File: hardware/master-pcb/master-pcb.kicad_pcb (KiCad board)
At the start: 4 copper layers, 84 x 69 mm, 37 parts, among them J1 RS-485 OUT, J2 INT IN 0-8, J4 UNDERGLOW OUT, SW1 PLAYER_ID, U1 Teensy 4.0, U2 THVD1429, U3 SN74AHCT125

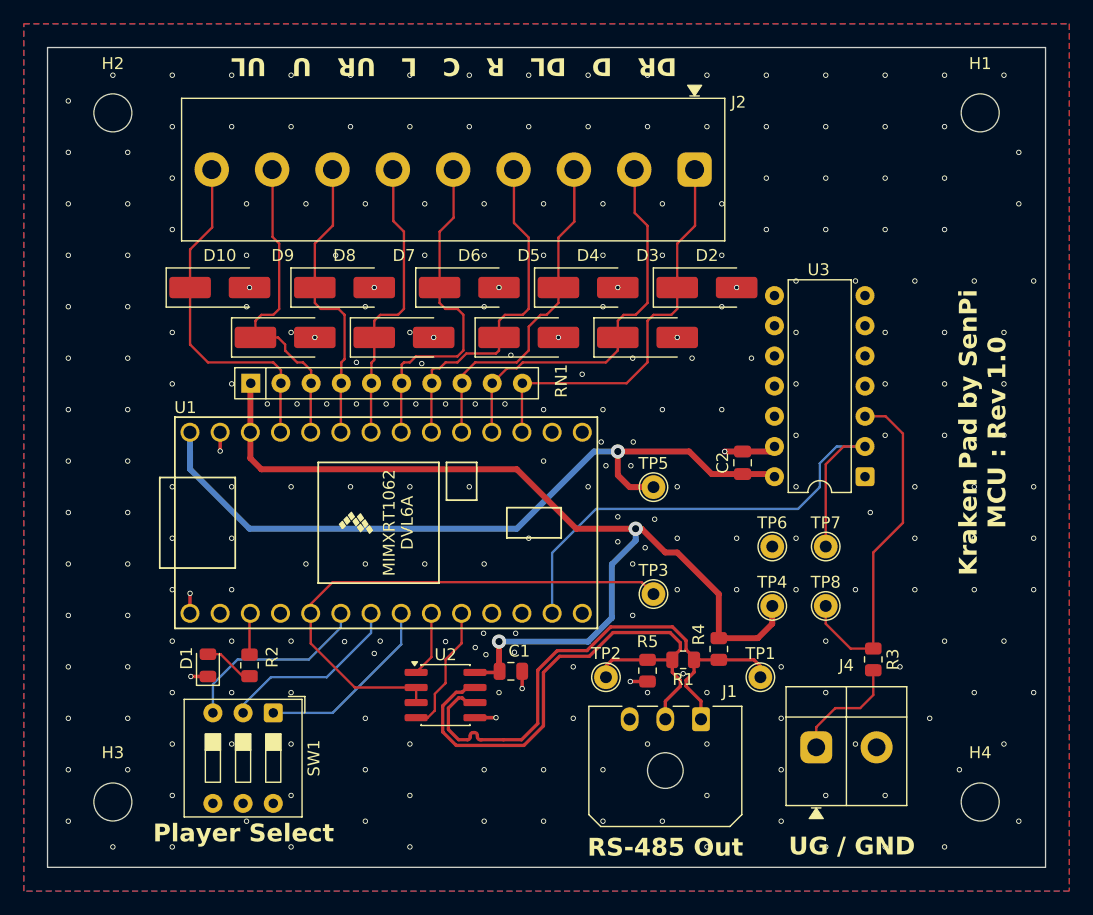
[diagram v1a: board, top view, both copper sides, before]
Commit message: Master: post-review rework — remove status LED, INT RC/TVS filter, pin reassign
- Remove status LED (D1, R2); Teensy onboard LED (pin 13) serves as status
- INT lines get two-stage protection: SMAJ5.0A TVS at the J2 entry + 330R
  series (R6-R14) + 1nF C0G RC (C3-C11) to GND on the Teensy-side node.
  Resolves review F3/F4 (series R makes the 5V-standoff TVS safe on the
  non-5V-tolerant Teensy pin; RC filters ESD/EMI). Pull-up stays Teensy-side.
- R15 10k pull-down on UNDERGLOW_DATA — defines U3 gate-A input LOW at boot
  (review F5)
- DIP -> GPIO 3/4/5, RS485_DE -> GPIO6; frees GPIO 0/1/2 and keeps Serial1
  (0/1) as the last spare hardware UART. RS-485 stays on Serial2 (7/8).
- ERC/DRC clean. docs/MASTER_PCB.md + BOM.md updated to match.
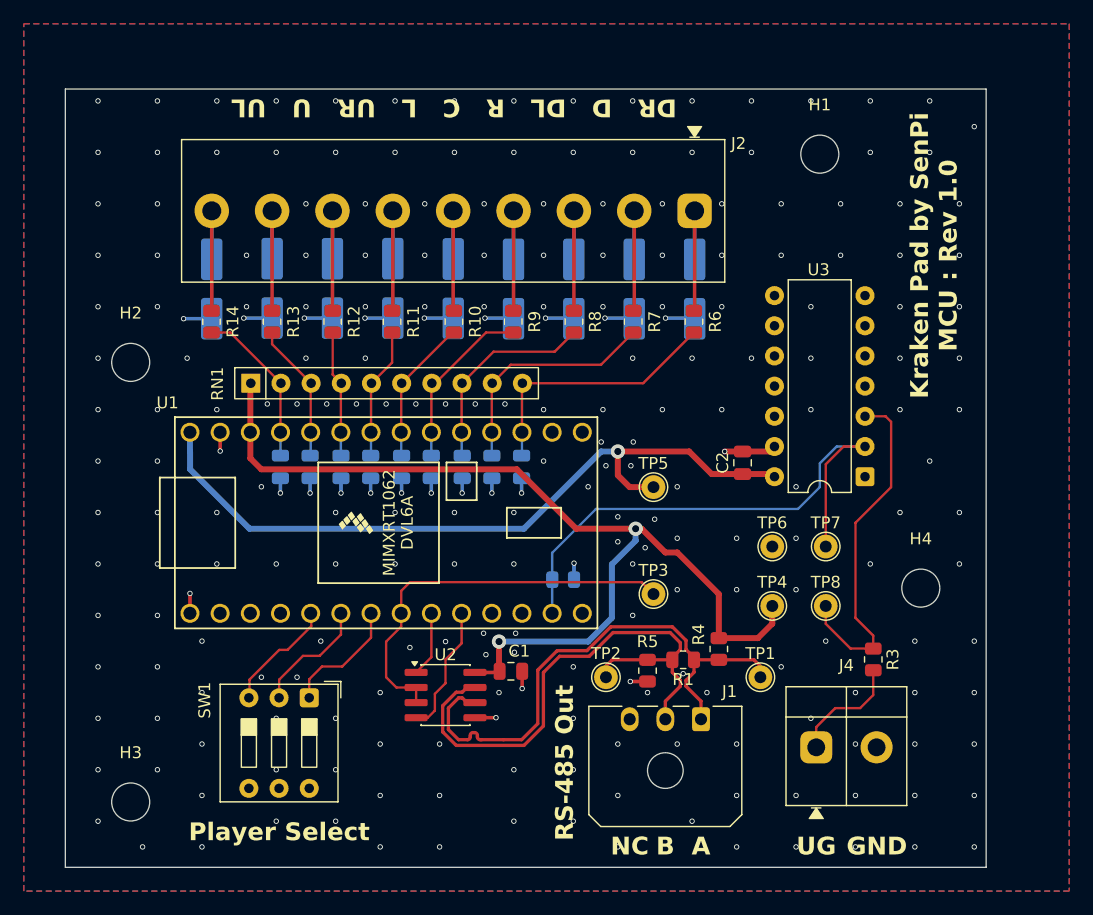
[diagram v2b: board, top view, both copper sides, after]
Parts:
- removed D1: STATUS, LED_SMD:LED_0805_2012Metric
- removed R2: 1k, Resistor_SMD:R_0805_2012Metric
- added C10: 1nF C0G, Capacitor_SMD:C_0805_2012Metric, B.Cu at (111.6, 109.3)
- added C11: 1nF C0G, Capacitor_SMD:C_0805_2012Metric, B.Cu at (109.1, 109.3)
- added C3: 1nF C0G, Capacitor_SMD:C_0805_2012Metric, B.Cu at (129.4, 109.3)
- added C4: 1nF C0G, Capacitor_SMD:C_0805_2012Metric, B.Cu at (126.9, 109.3)
- added C5: 1nF C0G, Capacitor_SMD:C_0805_2012Metric, B.Cu at (124.4, 109.3)
- added C6: 1nF C0G, Capacitor_SMD:C_0805_2012Metric, B.Cu at (121.8, 109.3)
- added C7: 1nF C0G, Capacitor_SMD:C_0805_2012Metric, B.Cu at (119.3, 109.3)
- added C8: 1nF C0G, Capacitor_SMD:C_0805_2012Metric, B.Cu at (116.7, 109.3)
- added C9: 1nF C0G, Capacitor_SMD:C_0805_2012Metric, B.Cu at (114.2, 109.3)
- added R10: 330R, Resistor_SMD:R_0805_2012Metric, F.Cu at (123.7, 97.1)
- added R11: 330R, Resistor_SMD:R_0805_2012Metric, F.Cu at (118.5, 97.1)
- added R12: 330R, Resistor_SMD:R_0805_2012Metric, F.Cu at (113.5, 97.1)
- added R13: 330R, Resistor_SMD:R_0805_2012Metric, F.Cu at (108.4, 97.1)
- added R14: 330R, Resistor_SMD:R_0805_2012Metric, F.Cu at (103.3, 97.1)
- added R15: 10k, Resistor_SMD:R_0805_2012Metric, B.Cu at (132.9, 118.8)
- added R6: 330R, Resistor_SMD:R_0805_2012Metric, F.Cu at (143.9, 97.1)
- added R7: 330R, Resistor_SMD:R_0805_2012Metric, F.Cu at (138.8, 97.1)
- added R8: 330R, Resistor_SMD:R_0805_2012Metric, F.Cu at (133.8, 97.1)
- added R9: 330R, Resistor_SMD:R_0805_2012Metric, F.Cu at (128.7, 97.1)
- D10, D2, D3, D4, D5, D6, D7, D8, D9: moved to B.Cu
- moved H2 21.1 mm to (96.5, 100.5)
- moved H4 18.7 mm to (163.0, 119.5)
- moved H1 13.9 mm to (154.5, 83.0)
- moved D9 4.27 mm to (108.4, 94.3), turned to -90 degrees
- moved D5 4.27 mm to (128.7, 94.3), turned to -90 degrees
- moved D7 4.23 mm to (118.6, 94.3), turned to -90 degrees
- moved D3 4.22 mm to (138.9, 94.3), turned to -90 degrees
- moved J2 3.47 mm to (144.0, 87.7)
- moved SW1 3.28 mm to (111.5, 128.7)
- moved H3 1.50 mm to (96.5, 137.5)
- moved D6 1.36 mm to (123.6, 94.3), turned to -90 degrees
- moved D4 1.20 mm to (133.8, 94.3), turned to -90 degrees
- moved D2 1.04 mm to (144.0, 94.3), turned to -90 degrees
- moved D8 1.02 mm to (113.5, 94.3), turned to -90 degrees
- moved D10 0.69 mm to (103.3, 94.3), turned to -90 degrees
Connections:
- D10 pad 1: INT_UL -> Net-(D10-K)
- D2 pad 1: INT_DR -> Net-(D2-K)
- D3 pad 1: INT_D -> Net-(D3-K)
- D4 pad 1: INT_DL -> Net-(D4-K)
- D5 pad 1: INT_R -> Net-(D5-K)
- D6 pad 1: INT_C -> Net-(D6-K)
- D7 pad 1: INT_L -> Net-(D7-K)
- D8 pad 1: INT_UR -> Net-(D8-K)
- D9 pad 1: INT_U -> Net-(D9-K)
- J2 pad 1: INT_DR -> Net-(D2-K)
- J2 pad 2: INT_D -> Net-(D3-K)
- J2 pad 3: INT_DL -> Net-(D4-K)
- J2 pad 4: INT_R -> Net-(D5-K)
- J2 pad 5: INT_C -> Net-(D6-K)
- J2 pad 6: INT_L -> Net-(D7-K)
- J2 pad 7: INT_UR -> Net-(D8-K)
- J2 pad 8: INT_U -> Net-(D9-K)
- J2 pad 9: INT_UL -> Net-(D10-K)
- U1 pad 3: /STATUS_LED -> unconnected-(U1-GPIO_1-Pad3)
- U1 pad 5: RS485_DE -> /DIP_ID2
- U1 pad 6: /DIP_ID2 -> /DIP_ID1
- U1 pad 7: /DIP_ID1 -> /DIP_ID0
- U1 pad 8: /DIP_ID0 -> RS485_DE
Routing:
- net GND: track 13.7 -> 46.3 mm, vias 264 -> 244
- net INT_C: track 28.5 -> 12.3 mm
- net INT_UL: track 29.3 -> 13.7 mm
- net INT_U: track 27.1 -> 11.8 mm
- net INT_R: track 29.2 -> 14.7 mm
- net INT_UR: track 24.8 -> 10.7 mm
- net INT_L: track 24.5 -> 11.1 mm
- net INT_D: track 33.1 -> 19.7 mm
- net Net-(D3-K): track 0.00 -> 12.5 mm
- net Net-(D2-K): track 0.00 -> 12.5 mm
- net Net-(D5-K): track 0.00 -> 12.5 mm
- net Net-(D10-K): track 0.00 -> 12.5 mm
- net Net-(D4-K): track 0.00 -> 12.5 mm
- net Net-(D6-K): track 0.00 -> 12.5 mm
- net Net-(D7-K): track 0.00 -> 12.5 mm
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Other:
- board size 84 x 69 mm -> 77.5 x 65.5 mm
- board text added: "A"
- board text added: "B"
- board text added: "GND"
- board text added: "NC"
- board text added: "UG"
- board text removed: "UG / GND"

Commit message: Master: RS-485 pair length-matched, RX/TX test points added
Same stackup as the panel (JLC04161H-7628), so the same 120-ohm target
geometry applies. The pair was already at W=0.15/S=0.2 -- it landed on the
right answer via the 0.15mm data-trace convention rather than by calculation
-- so only the skew needed work.

- /RS485+ and /RS485- now 45.39mm each: 0.000mm skew (was 0.60mm). F.Cu only,
  zero vias, ~119 ohm. Netclass diff-pair width corrected 0.2787 -> 0.15 and
  the stale USB pair class dropped (the Teensy handles USB internally; nothing
  USB is routed on this board).
- TP9 (RS485_RX) and TP10 (RS485_TX) added, giving probe access to the full
  transceiver interface alongside TP1/TP2/TP3 (A/B/DE).
- ~69% of the run is coupled at 0.2mm; the rest fans out to reach pads that
  are farther apart than the pair pitch (U2 pins 6/7, J1 Micro-Fit, R1,
  TP1/TP2). That is unavoidable and inconsequential at 1 Mbps -- documented as
  do-not-fix so it is not "corrected" later.

Also recorded: both inner layers are GND (GND_1/GND_2), unlike the panel's
GND/power split, so there is no reference-plane-type change anywhere on this
board.

Verified with all three ignored severities lifted, --severity-all
--schematic-parity --refill-zones: 0 violations, 0 unconnected, ERC 0. Only 3
cosmetic footprint_filters_mismatch notes (Euroblock, MRR52, DIP-3).
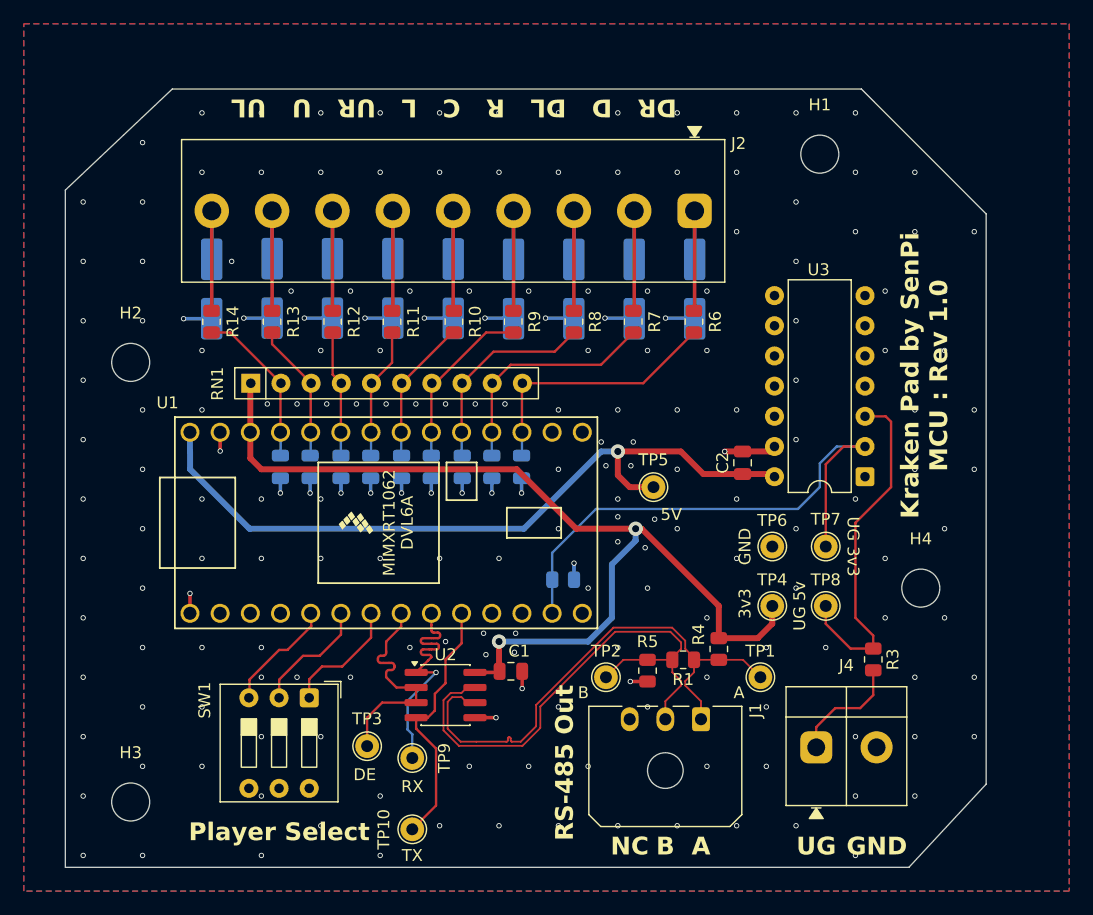
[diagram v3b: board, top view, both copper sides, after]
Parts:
- added TP10: RS-485 TX, TestPoint:TestPoint_THTPad_D2.0mm_Drill1.0mm, F.Cu at (120.2, 139.8)
- added TP9: RS-485 RX, TestPoint:TestPoint_THTPad_D2.0mm_Drill1.0mm, F.Cu at (120.2, 133.8)
- moved TP3 27.3 mm to (116.4, 132.8)
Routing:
- net RS485_RX: track 5.51 -> 20.9 mm, vias 0 -> 1
- net RS485_DE: track 33.9 -> 19.2 mm
- net RS485_TX: track 10.9 -> 21.9 mm
- net /RS485-: track 47.2 -> 45.4 mm
- net /RS485+: track 47.2 -> 45.4 mm
- net +3.3VDC: track 84.0 -> 83.3 mm
- net GND: vias 244 -> 201
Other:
- outline, holes or cut-outs redrawn
- board text added: "3v3"
- board text added: "5V"
- board text added: "DE"
- board text added: "RX"
- board text added: "TX"
- board text added: "UG 3v3"
- board text added: "UG 5v"

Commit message: Both boards: J9/J4 to the vendor WJ500V land pattern; WS2815 cap question closed
Terminal blocks now use the footprint published by the manufacturer of the part
we actually buy (KANGNEX WJ500V-5.08-2P, LCSC C8465), pulled via easyeda2kicad,
replacing the hand-built Adam Tech MRR52 pattern:
- new panel-pcb/master-pcb:TerminalBlock_WJ500V-5.08-2P (hole 1.30mm per the
  vendor recommendation vs our 1.50mm, pad 2.00mm, origin centred between pins)
  plus the vendor 3D model, which supersedes the Phoenix MKDS stand-in
- panel J9 and master J4 reassigned, re-placed and re-routed
- part metadata follows: MPN WJ500V-5.08-2P, LCSC C8465, datasheet to the LCSC
  page, stale DigiKey fields dropped

Pitch (5.08mm) and body envelope (10.16 x 10.16mm) came out of the vendor data
matching our drawing-derived numbers, so that part of the physical-verification
item is closed without parts in hand; pin-1 orientation still wants an eyeball
on arrival.

Checklist: WS2815 5V bench test waived (not worth buying parts; the substantive
check was the datasheet-variant confirm, and VIH 2.7V min is a spec guarantee).
Per-LED pin-1 caps C22-C49 CLOSED as correct — the original 2018 WS2815 doc and
WS2815B-V3 both give pin 1 as "IC POWER SUPPLY, Suspended or connected with a
filter capacitor to GROUND"; our V1 doc is the outlier calling it NC. Paper does
not prove V1 silicon brings that rail out, but a 100nF is no DC load, so the cap
is inert at worst. No per-LED VDD decoupling is wanted: the channels are
constant-current, and the vendor states no extra components are needed.

DRC 0 / schematic-parity 0 / ERC 0 on both boards, zero exclusions.
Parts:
- J4: footprint master-pcb:TerminalBlock_MRR52-5.08-2P -> master-pcb:TerminalBlock_WJ500V-5.08-2P
- moved J4 2.53 mm to (156.7, 132.9), turned to 180 degrees
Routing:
- net Net-(J4-Pin_1): track 9.71 -> 6.60 mm
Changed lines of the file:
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@@
 		)
 	)
-	(footprint "master-pcb:TerminalBlock_MRR52-5.08-2P"
+	(footprint "master-pcb:TerminalBlock_WJ500V-5.08-2P"
 		(layer "F.Cu")
-		(at 154.2 132.9)
-		(descr "Adam Tech MRR52-5.08-V, 2-position Eurostyle PCB screw terminal block, 5.08mm pitch. Dims from datasheet 375571 (2020/01): body 10.16 x 10.00mm, pin row 5.10mm from wire-entry face, PCB hole Rec. dia 1.50mm.")
-		(tags "terminal block MRR52 euroblock 5.08mm screw")
+		(at 156.7275 132.9 180)
+		(descr "KANGNEX WJ500V-5.08-2P, 2-position Eurostyle PCB screw terminal block, 5.08mm pitch (LCSC C8465). Land pattern and 3D model are the VENDOR's own, pulled via easyeda2kicad 2026-07-26 -- this replaces the hand-built TerminalBlock_MRR52-5.08-2P (Adam Tech drawing, 1.5mm holes) now that the part is sourced from LCSC. Recommended hole 1.30mm, pad 2.00mm (annular ring 0.35mm, vs the 0.15mm .dru minimum). Body 10.16 x 10.16mm; the pin row is NOT centred -- 5.64mm to the wire-entry face (-Y, marked by the silk arrows) and 4.52mm to the back. Origin is centred between the two pins.")
+		(tags "terminal block WJ500V euroblock 5.08mm screw KANGNEX")
 		(property "Reference" "J4"
-			(at 2.54 -6.9 0)
+			(at 6.2275 -4.9 90)
 			(layer "F.SilkS")
 			(effects
@@
 		)
 		(property "Value" "UNDERGLOW OUT"
-			(at 2.54 6.4 0)
+			(at 0 5.9 0)
 			(layer "F.Fab")
 			(effects
@@
 			)
 		)
-		(property "Datasheet" "https://dcomponents.com/uploads/375571_MRR52-5.08-V.pdf"
+		(property "Datasheet" "https://www.lcsc.com/product-detail/C8465.html"
 			(at 0 0 0)
 			(layer "F.Fab")
@@
 			)
 		)
-		(property "Description" "Adam Tech MRR522-5.08-V, 2P 5.08mm top-entry screw terminal: GND + LED-DATA-OUT (5V logic). UI-gated; no sense pin"
+		(property "Description" "KANGNEX WJ500V-5.08-2P (LCSC C8465), 2P 5.08mm top-entry screw terminal: GND + LED-DATA-OUT (5V logic). UI-gated; no sense pin"
 			(at 0 0 0)
 			(layer "F.Fab")
@@
 			)
 		)
-		(property "LCSC" ""
+		(property "LCSC" "C8465"
 			(at 0 0 0)
-			(unlocked yes)
 			(layer "F.Fab")
 			(hide yes)
 			(effects
 				(font
-					(size 1 1)
-					(thickness 0.15)
-				)
-			)
-		)
-		(property "MPN" "MRR522-5.08-V"
-			(at 0 0 0)
-			(unlocked yes)
-			(layer "F.Fab")
-			(hide yes)
-			(effects
-				(font
-					(size 1 1)
+					(size 1.27 1.27)
 					(thickness 0.15)
 				)
 			)
 		)
-		(property "DigiKey" "5245-MRR522-5.08-V-ND"
-			(at 0 0 0)
+		(property "MPN" "WJ500V-5.08-2P"
+			(at 0 0 180)
 			(unlocked yes)
 			(layer "F.Fab")
@@
 		(duplicate_pad_numbers_are_jumpers no)
 		(fp_line
-			(start -2.54 -5.1)
-			(end 7.62 -5.1)
-			(stroke
-				(width 0.12)
-				(type solid)
-			)
-			(layer "F.SilkS")
-		)
-		(fp_line
-			(start -2.54 -2.55)
-			(end 7.62 -2.55)
+			(start 5.08 4.52)
+			(end -5.08 4.52)
 			(stroke
 				(width 0.12)
@@
 		)
 		(fp_line
-			(start -2.54 4.9)
-			(end -2.54 -5.1)
+			(start 5.08 -5.64)
+			(end 5.08 4.52)
 			(stroke
 				(width 0.12)
@@
 		)
 		(fp_line
-			(start 0.4 5.1)
-			(end -0.4 5.1)
+			(start 0 -5.64)
+			(end 0 4.52)
 			(stroke
 				(width 0.12)
@@
 		)
 		(fp_line
-			(start 2.54 -5.1)
-			(end 2.54 4.9)
+			(start -5.08 4.52)
+			(end -5.08 -5.64)
 			(stroke
 				(width 0.12)
@@
 		)
 		(fp_line
-			(start 7.62 -5.1)
-			(end 7.62 4.9)
+			(start -5.08 -2.55)
+			(end 5.08 -2.55)
 			(stroke
 				(width 0.12)
@@
 		)
 		(fp_line
-			(start 7.62 4.9)
-			(end -2.54 4.9)
+			(start -5.08 -5.64)
+			(end 5.08 -5.64)
 			(stroke
 				(width 0.12)
@@
 			(layer "F.SilkS")
 		)
-		(fp_poly
-			(pts
-				(xy -0.6 6) (xy 0 5.1) (xy 0.6 6)
-			)
+		(fp_circle
+			(center -6.1 4.52)
+			(end -5.85 4.52)
 			(stroke
-				(width 0.1)
+				(width 0.3)
 				(type solid)
 			)
@@
 		)
 		(fp_line
-			(start -2.79 -5.35)
-			(end 7.87 -5.35)
+			(start 5.33 4.77)
+			(end -5.33 4.77)
 			(stroke
 				(width 0.05)
@@
 		)
 		(fp_line
-			(start -2.79 5.15)
-			(end -2.79 -5.35)
+			(start 5.33 -5.89)
+			(end 5.33 4.77)
 			(stroke
 				(width 0.05)
@@
 		)
 		(fp_line
-			(start 7.87 -5.35)
-			(end 7.87 5.15)
+			(start -5.33 4.77)
+			(end -5.33 -5.89)
 			(stroke
 				(width 0.05)
@@
 		)
 		(fp_line
-			(start 7.87 5.15)
-			(end -2.79 5.15)
+			(start -5.33 -5.89)
+			(end 5.33 -5.89)
 			(stroke
 				(width 0.05)
@@
 		)
 		(fp_line
-			(start -2.54 -5.1)
-			(end 7.62 -5.1)
+			(start 5.08 4.52)
+			(end -5.08 4.52)
 			(stroke
 				(width 0.1)
@@
 		)
 		(fp_line
-			(start -2.54 4.9)
-			(end -2.54 -5.1)
+			(start 5.08 -5.64)
+			(end 5.08 4.52)
 			(stroke
 				(width 0.1)
@@
 		)
 		(fp_line
-			(start 7.62 -5.1)
-			(end 7.62 4.9)
+			(start -5.08 4.52)
+			(end -5.08 -5.64)
 			(stroke
 				(width 0.1)
@@
 		)
 		(fp_line
-			(start 7.62 4.9)
-			(end -2.54 4.9)
+			(start -5.08 -5.64)
+			(end 5.08 -5.64)
 			(stroke
 				(width 0.1)
@@
 		)
 		(fp_circle
-			(center 0 -2.9)
-			(end 1.5 -2.9)
+			(center 2.54 -2.9)
+			(end 4.04 -2.9)
 			(stroke
 				(width 0.1)
@@
 		)
 		(fp_circle
-			(center 5.08 -2.9)
-			(end 6.58 -2.9)
+			(center -2.54 -2.9)
+			(end -1.04 -2.9)
 			(stroke
 				(width 0.1)
@@
 		)
 		(fp_text user "${REFERENCE}"
-			(at 2.54 0 0)
+			(at 0 1.9 0)
 			(layer "F.Fab")
 			(effects
@@
 			)
 		)
-		(pad "1" thru_hole roundrect
-			(at 0 0)
-			(size 2.7 2.7)
-			(drill 1.5)
+		(pad "1" thru_hole circle
+			(at -2.54 0 180)
+			(size 2 2)
+			(drill 1.3)
 			(layers "*.Cu" "*.Mask")
 			(remove_unused_layers no)
-			(roundrect_rratio 0.25)
 			(net "Net-(J4-Pin_1)")
 			(pinfunction "Pin_1_1")
@@
 		)
 		(pad "2" thru_hole circle
-			(at 5.08 0)
-			(size 2.7 2.7)
-			(drill 1.5)
+			(at 2.54 0 180)
+			(size 2 2)
+			(drill 1.3)
 			(layers "*.Cu" "*.Mask")
 			(remove_unused_layers no)
@@
 		)
 		(embedded_fonts no)
-		(model "${KICAD10_3DMODEL_DIR}/TerminalBlock_Phoenix.3dshapes/TerminalBlock_Phoenix_MKDS-1,5-2-5.08_1x02_P5.08mm_Horizontal.step"
+		(model "${KIPRJMOD}/3dmodels/WJ500V-5.08-2P.step"
 			(offset
-				(xyz 0 0 0)
+				(xyz 2.84 0 0)
 			)
 			(scale
@@
 	)
 	(segment
-		(start 159 128.5)
-		(end 159 126.4125)
-		(width 0.2)
-		(layer "F.Cu")
-		(net "Net-(J4-Pin_1)")
-	)
-	(segment
-		(start 154.2 131.2)
-		(end 155.8 129.6)
-		(width 0.2)
-		(layer "F.Cu")
-		(net "Net-(J4-Pin_1)")
-	)
-	(segment
-		(start 157.9 129.6)
-		(end 159 128.5)
+		(start 159 129.6)
+		(end 159.2675 129.8675)
 		(width 0.2)
 		(layer "F.Cu")
@@
 	)
 	(segment
-		(start 155.8 129.6)
-		(end 157.9 129.6)
+		(start 159 126.4125)
+		(end 159 129.6)
 		(width 0.2)
 		(layer "F.Cu")
@@
 	)
 	(segment
-		(start 154.2 132.9)
-		(end 154.2 131.2)
+		(start 159.2675 129.8675)
+		(end 159.2675 132.9)
 		(width 0.2)
 		(layer "F.Cu")
